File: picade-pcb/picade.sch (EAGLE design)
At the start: 53 parts

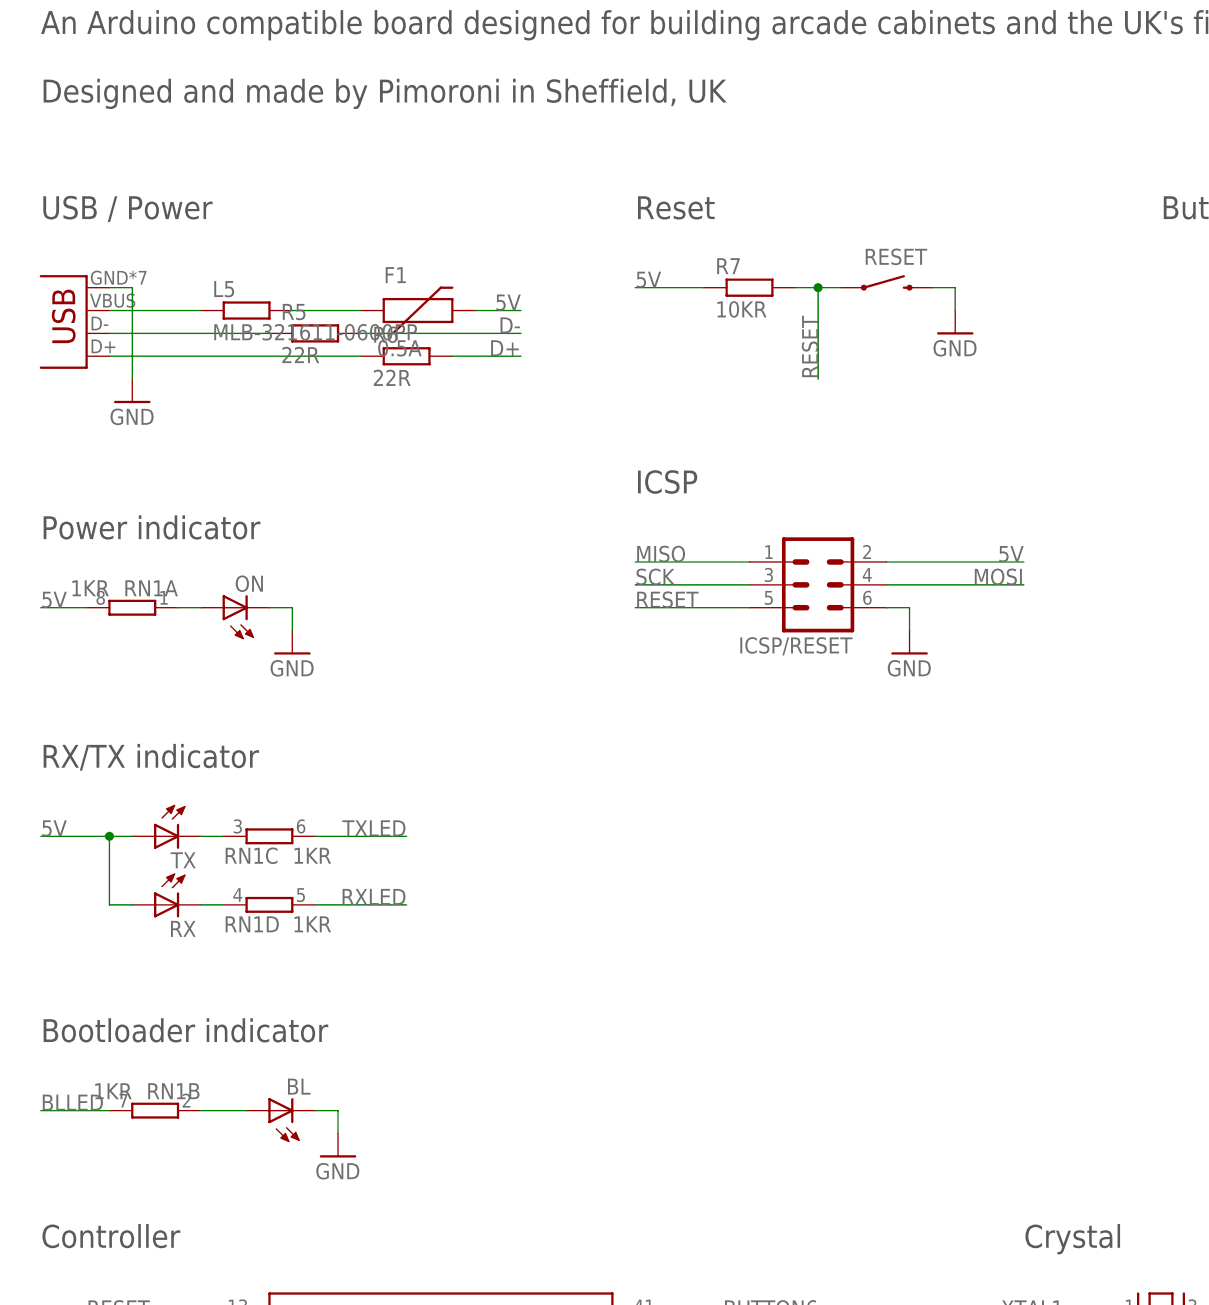
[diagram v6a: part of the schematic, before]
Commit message: Added USB shield decoupling
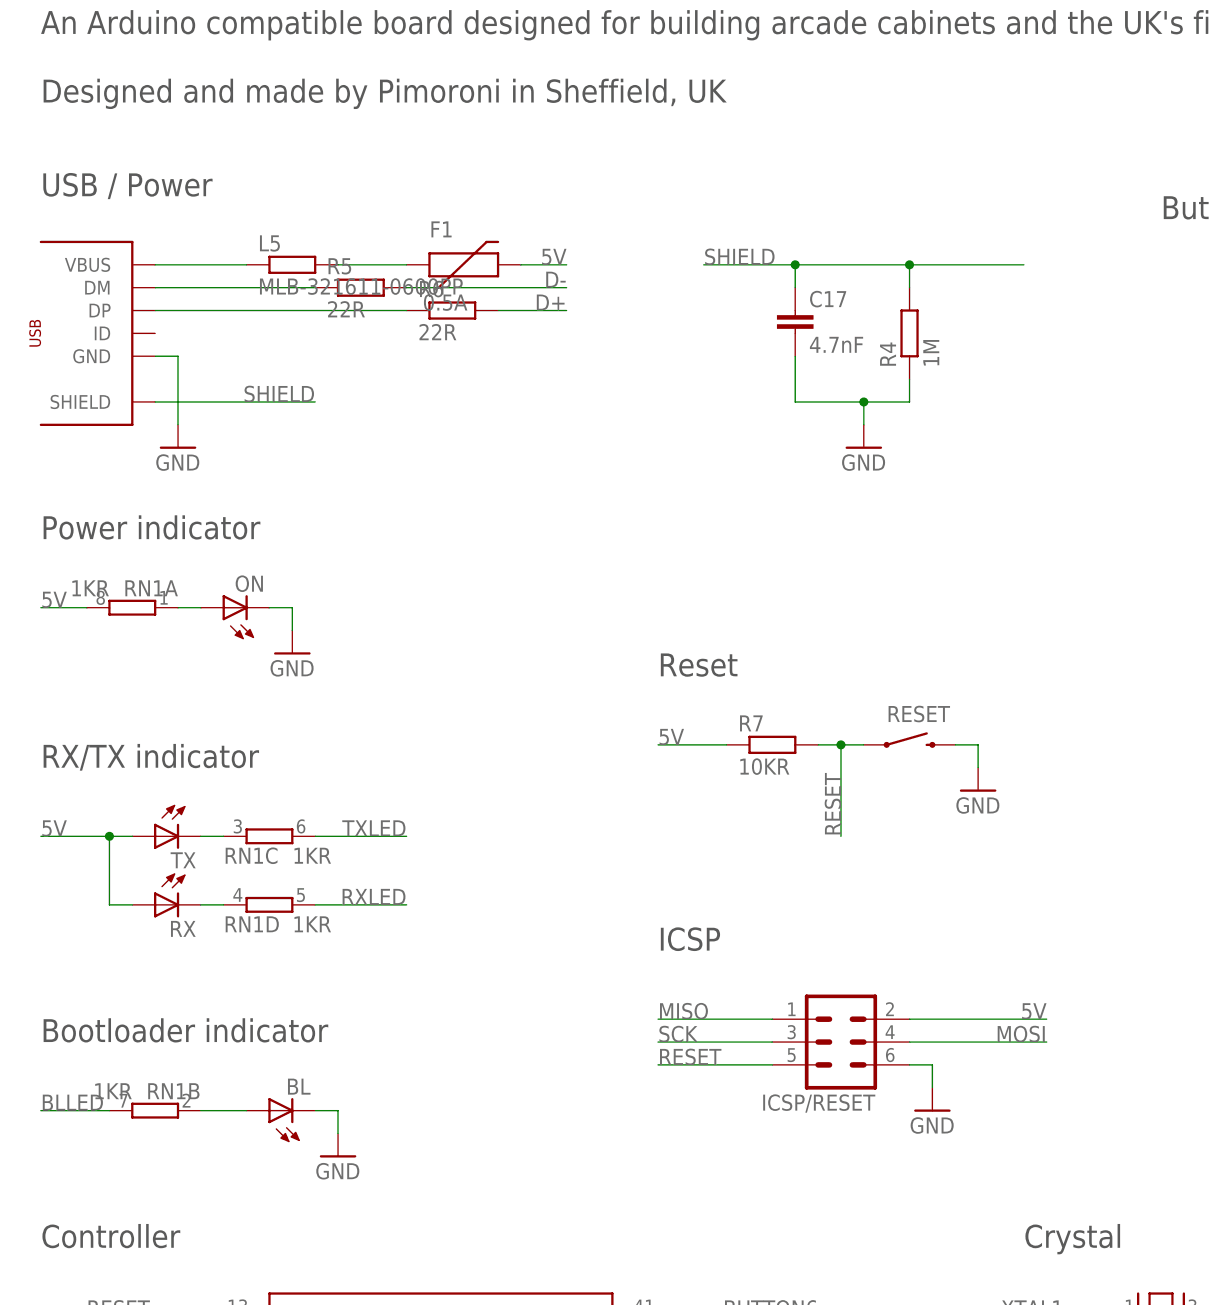
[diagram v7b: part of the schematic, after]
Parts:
- removed USB: USB-MICROB, pimoroni:USB-MICROB
- added C17: 4.7nF, resistor:C-EUC0603K
- added R4: 1M, resistor:R-EU_R0603
- added U$13: USBMICROB, pimoroni-connectors:USBMICROB
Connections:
- new net SHIELD: C17.1, R4.2, U$13.SHIELD
- net GND: now also C17.2, R4.1, U$13.GND; no longer USB.GND
- net N$3: now also U$13.DM; no longer USB.D-
- net N$4: now also U$13.DP; no longer USB.D+
- net VBUS: now also U$13.VBUS; no longer USB.VBUS
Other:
- moved on the sheet: F1, ICSP/RESET, L5, R5, R6, R7, RESET
